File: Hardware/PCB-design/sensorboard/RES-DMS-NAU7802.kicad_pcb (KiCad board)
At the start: 2 copper layers, 32 x 32 mm, 43 parts, among them J1 Conn_01x05_Female, J2 straingauge, J3 straingauge, J4 straingauge, J5 straingauge, J6 straingauge, J7 straingauge, J8 straingauge, J9 straingauge, U1 NAU7802-SGI

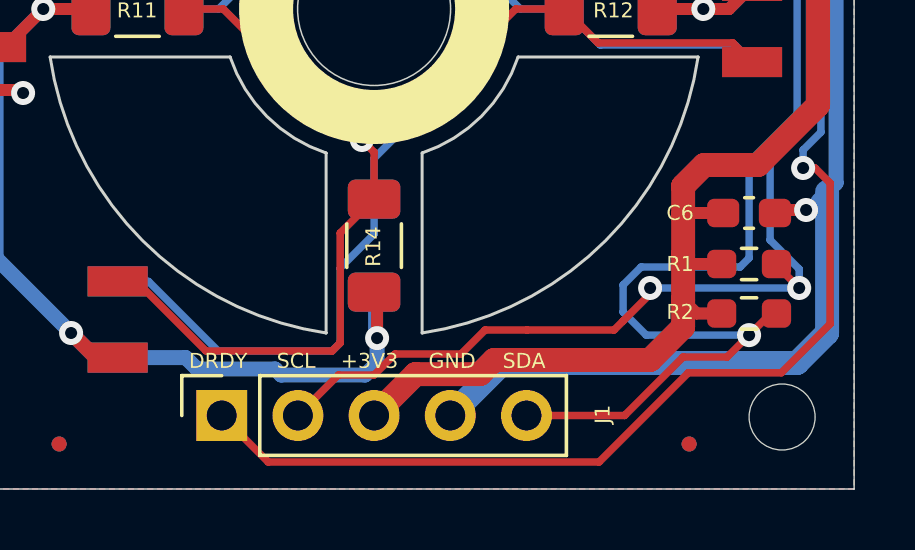
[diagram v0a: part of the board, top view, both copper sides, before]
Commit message: Changed sensorboard connector to 6pins with 1.27mm spacing (matching the IDC cable)
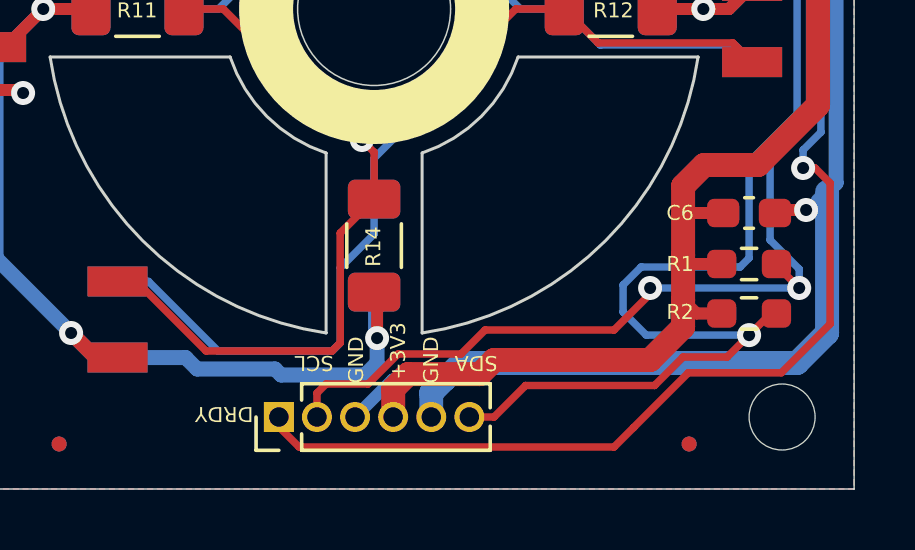
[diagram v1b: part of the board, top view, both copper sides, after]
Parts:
- J1: value Conn_01x05_Female -> Conn_01x06; footprint Connector_PinSocket_2.54mm:PinSocket_1x05_P2.54mm_Vertical -> Connector_PinHeader_1.27mm:PinHeader_1x06_P1.27mm_Vertical
- moved LOGO1 20.5 mm to (126.1, 93.3), turned to 0 degrees
- moved J1 1.91 mm to (112.8, 117.6)
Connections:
- J1 pad 3: +3.3V -> GND
- J1 pad 4: GND -> +3.3V
- J1 pad 5: /SDA -> GND
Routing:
- net GND: track 34.1 -> 38.7 mm
- net /DRDY: track 48.5 -> 46.4 mm
- net /SDA: track 45.7 -> 47.6 mm
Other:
- board text added: "RES-DMS v1.0 NAU7802 Aigner 10.2022"
- board text removed: "RES-DMS v0.1 NAU7802 Aigner 07.2022"

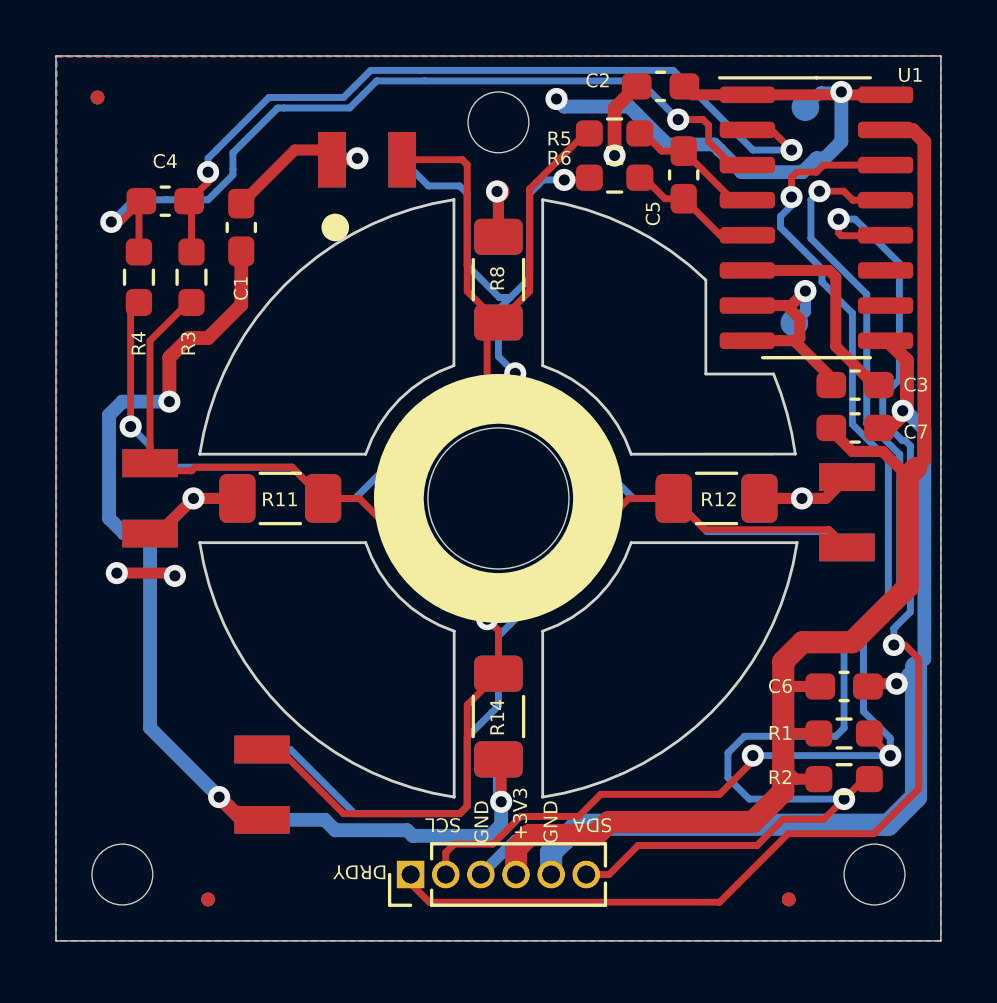
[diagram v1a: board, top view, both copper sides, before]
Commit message: Changed connector orientation
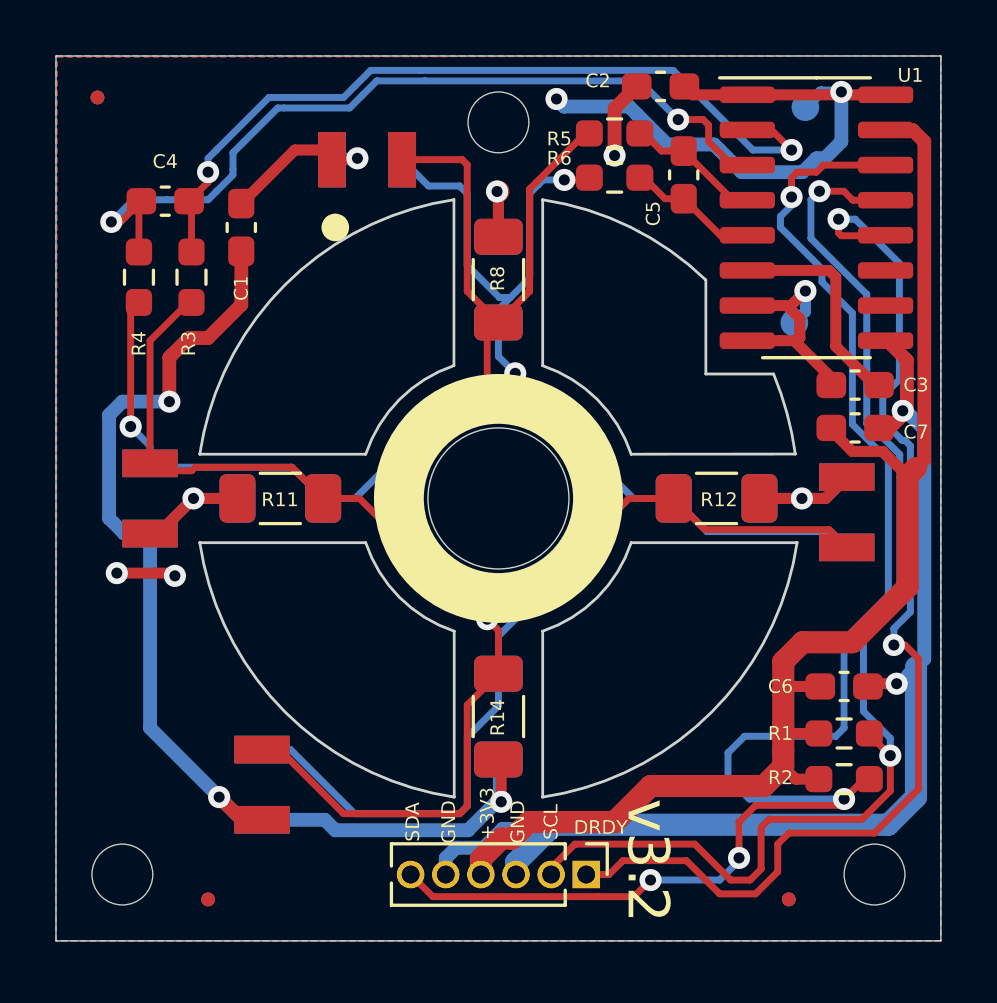
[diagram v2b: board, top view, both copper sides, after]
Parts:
- moved J1 6.35 mm to (119.2, 117.6), turned to -90 degrees
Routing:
- net /SDA: track 47.6 -> 55.4 mm, vias 2 -> 4
- net /DRDY: track 46.4 -> 40.6 mm
- net GND: track 38.7 -> 41.1 mm
- net /SCL: track 44.9 -> 43.4 mm, vias 3 -> 2
- net +3.3VADC: track 72.2 -> 71.5 mm
- net +3.3V: track 47.4 -> 47.9 mm
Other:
- board text added: "RES-DMS v3.2 NAU7802 Aigner 11.2022"
- board text added: "v3.2"
- board text removed: "RES-DMS v1.0 NAU7802 Aigner 10.2022"
